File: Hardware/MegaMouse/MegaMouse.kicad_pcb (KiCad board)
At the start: 2 copper layers, 93 x 120.5 mm, 12 parts, among them J201 Motor, J301 Motor, U101 ATmega328P-A, U102 STATE, U201 DRV8871DDA, U301 DRV8871DDA

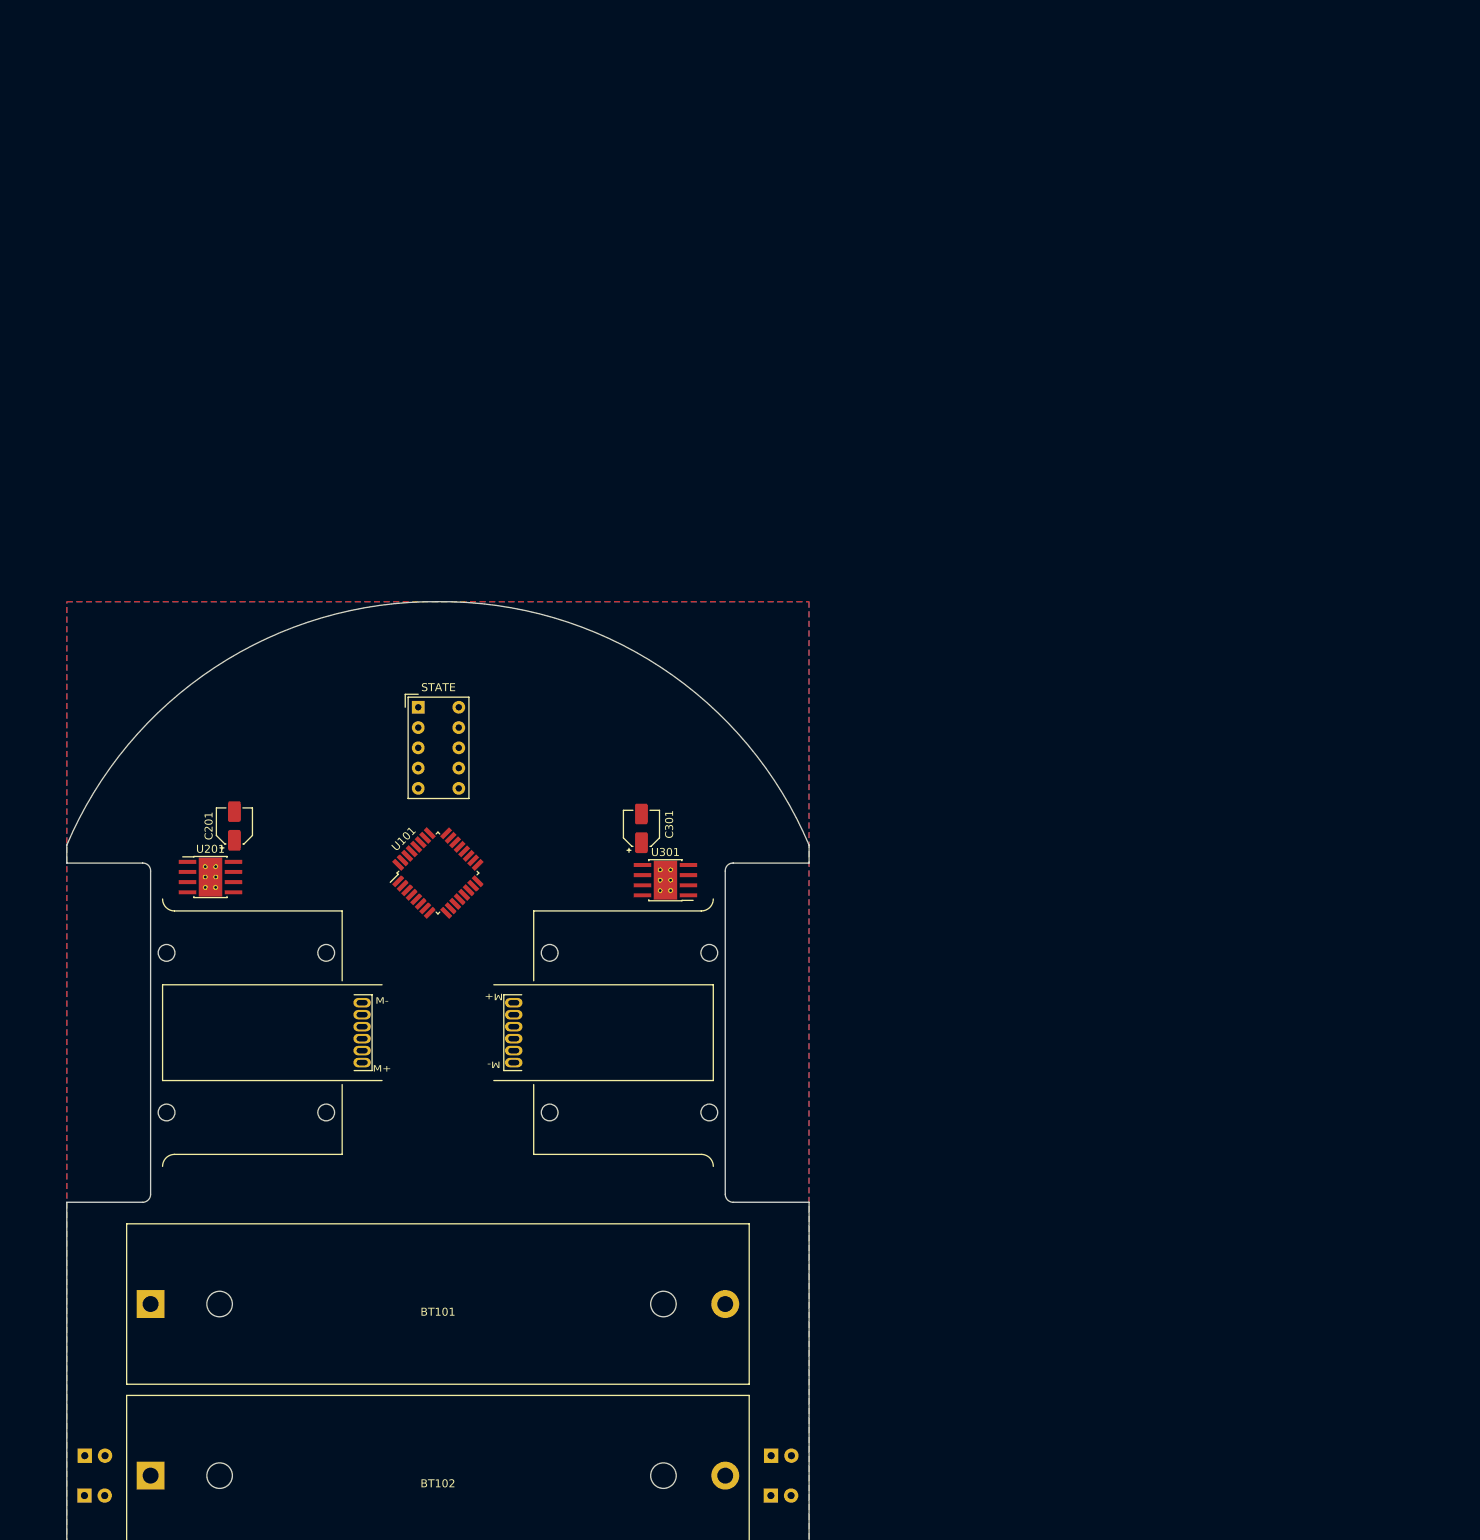
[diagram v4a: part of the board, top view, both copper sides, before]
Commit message: Add second layer
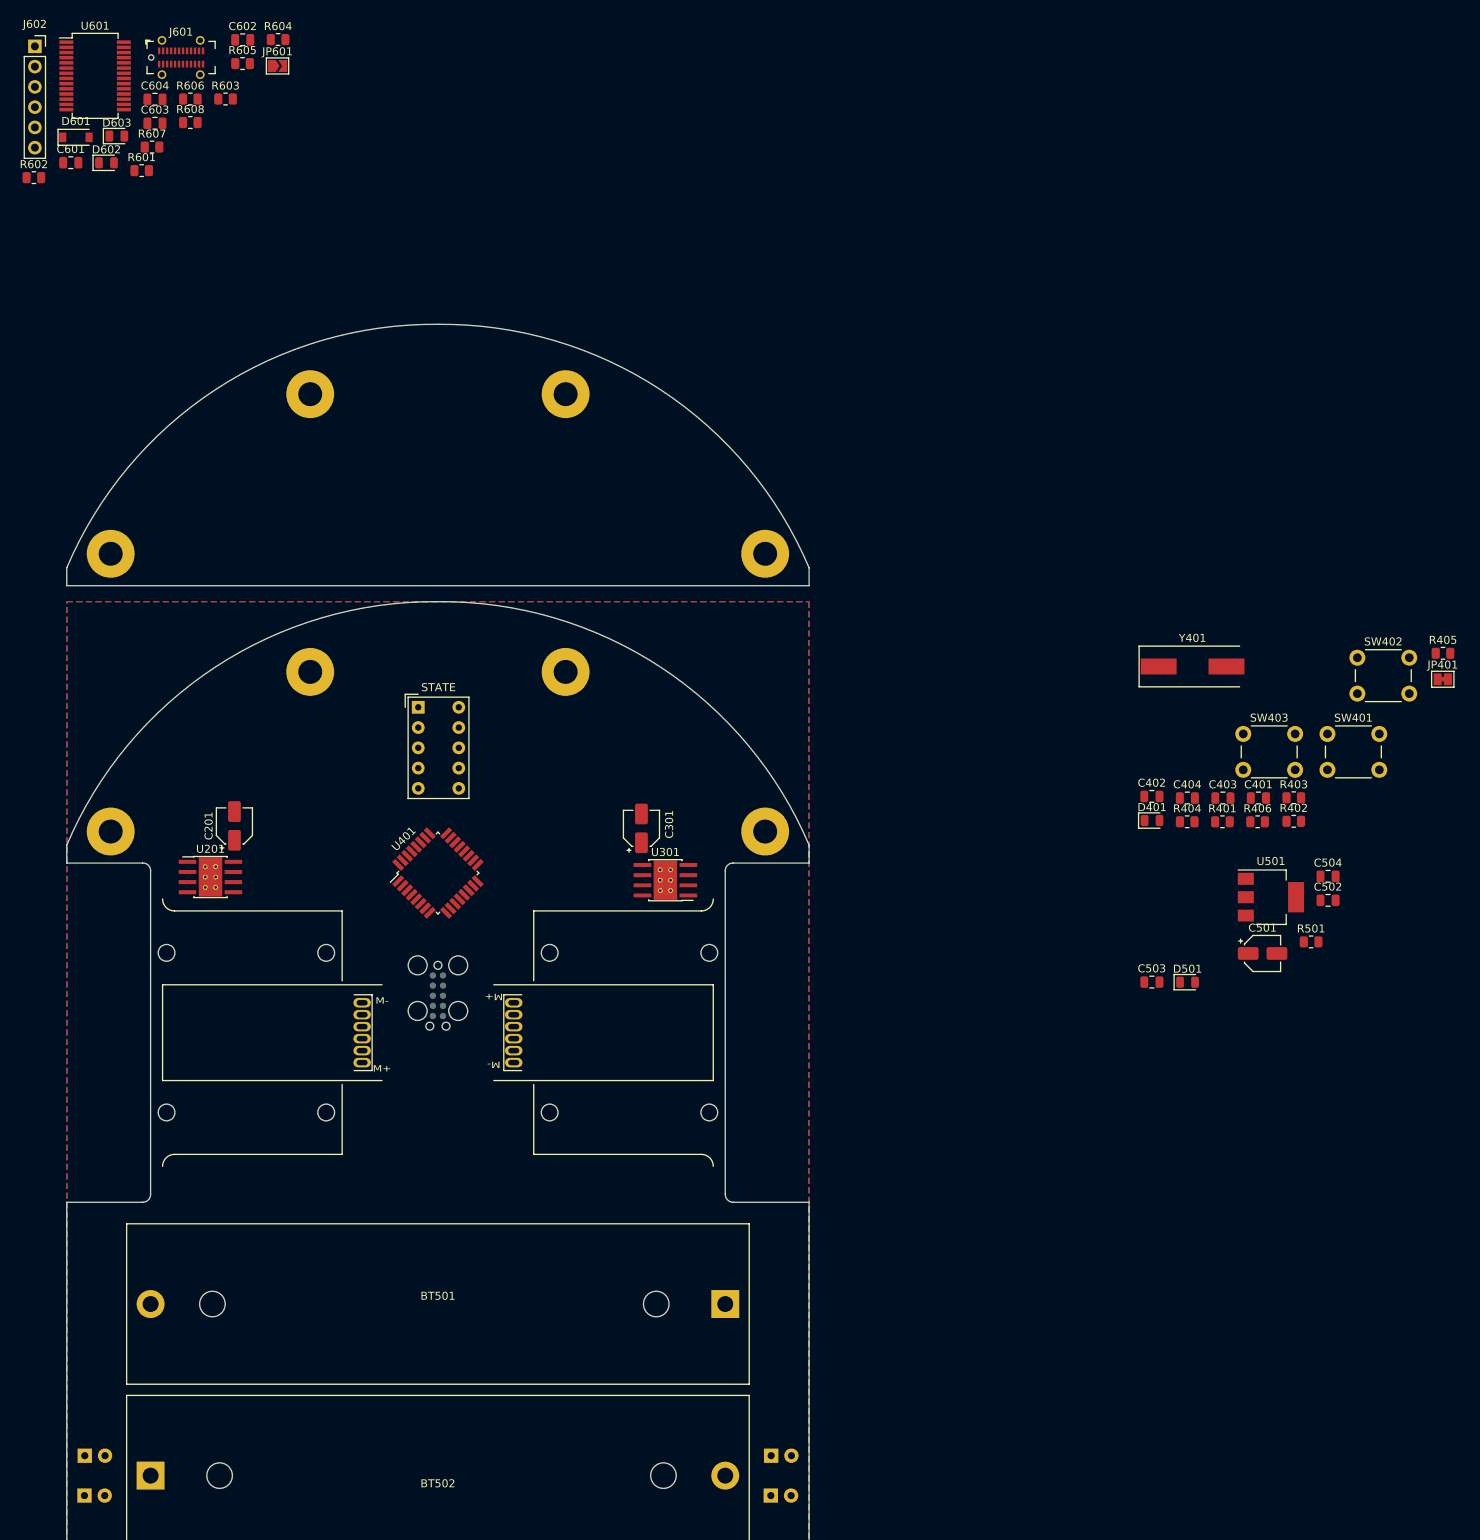
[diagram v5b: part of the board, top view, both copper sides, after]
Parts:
- removed BT101: Cell1, Battery:BatteryHolder_MPD_BH-18650-PC2
- removed BT102: Cell2, Battery:BatteryHolder_MPD_BH-18650-PC2
- removed the U101 at (0.00, -20.0)
- added BT501: Cell1, Battery:BatteryHolder_MPD_BH-18650-PC2, F.Cu at (36.0, 34.0)
- added BT502: Cell2, Battery:BatteryHolder_MPD_BH-18650-PC2, F.Cu at (-36.0, 55.5)
- added C401: 100nF, Capacitor_SMD:C_0805_2012Metric, F.Cu at (102.8, -29.4)
- added C402: 100nF, Capacitor_SMD:C_0805_2012Metric, F.Cu at (89.5, -29.6)
- added C403: 22pf, Capacitor_SMD:C_0805_2012Metric, F.Cu at (98.3, -29.4)
- added C404: 22pf, Capacitor_SMD:C_0805_2012Metric, F.Cu at (93.9, -29.4)
- added C501: 10uf, Capacitor_SMD:CP_Elec_4x3, F.Cu at (103.3, -9.92)
- added C502: 100nF, Capacitor_SMD:C_0805_2012Metric, F.Cu at (111.5, -16.6)
- added C503: 100nF, Capacitor_SMD:C_0805_2012Metric, F.Cu at (89.5, -6.34)
- added C504: 1uF, Capacitor_SMD:C_0805_2012Metric, F.Cu at (111.5, -19.6)
- added C601: 100nF, Capacitor_SMD:C_0805_2012Metric, F.Cu at (-46.0, -109.0)
- added C602: 100nF, Capacitor_SMD:C_0805_2012Metric, F.Cu at (-24.5, -124.4)
- added C603: 100nF, Capacitor_SMD:C_0805_2012Metric, F.Cu at (-35.5, -113.9)
- added C604: 100nF, Capacitor_SMD:C_0805_2012Metric, F.Cu at (-35.5, -117.0)
- added D401: STAT, LED_SMD:LED_0805_2012Metric, F.Cu at (89.5, -26.6)
- added D501: PWR, LED_SMD:LED_0805_2012Metric, F.Cu at (93.9, -6.33)
- added D601: MBR0520, Diode_SMD:D_SOD-123, F.Cu at (-45.4, -112.2)
- added D602: RX, LED_SMD:LED_0805_2012Metric, F.Cu at (-41.5, -109.0)
- added D603: TX, LED_SMD:LED_0805_2012Metric, F.Cu at (-40.2, -112.3)
- added H101: MountingHole_Pad, MountingHole:MountingHole_3mm_Pad, F.Cu at (41.0, -25.2)
- added H102: MountingHole_Pad, MountingHole:MountingHole_3mm_Pad, F.Cu at (-16.0, -45.2)
- added H103: MountingHole_Pad, MountingHole:MountingHole_3mm_Pad, F.Cu at (-41.0, -25.2)
- added H104: MountingHole_Pad, MountingHole:MountingHole_3mm_Pad, F.Cu at (16.0, -45.2)
- added H601: MountingHole_Pad, MountingHole:MountingHole_3mm_Pad, F.Cu at (41.0, -60.0)
- added H602: MountingHole_Pad, MountingHole:MountingHole_3mm_Pad, F.Cu at (16.0, -80.0)
- added H603: MountingHole_Pad, MountingHole:MountingHole_3mm_Pad, F.Cu at (-41.0, -60.0)
- added H604: MountingHole_Pad, MountingHole:MountingHole_3mm_Pad, F.Cu at (-16.0, -80.0)
- added J401: ICSP, Connector:Tag-Connect_TC2050-IDC-FP_2x05_P1.27mm_Vertical, B.Cu at (0.00, -4.62)
- added J601: USBC, Connector_USB:USB_C_Receptacle_GCT_USB4115-03-C, F.Cu at (-32.2, -122.2)
- added J602: PROG, Connector_PinSocket_2.54mm:PinSocket_1x06_P2.54mm_Vertical, F.Cu at (-50.5, -123.6)
- added JP401: RSTBridge, Jumper:SolderJumper-2_P1.3mm_Bridged_Pad1.0x1.5mm, F.Cu at (125.9, -44.3)
- added JP601: SolderJumper_2_Open, Jumper:SolderJumper-2_P1.3mm_Open_TrianglePad1.0x1.5mm, F.Cu at (-20.1, -121.1)
- added R401: 1K, Resistor_SMD:R_0805_2012Metric, F.Cu at (98.3, -26.4)
- added R402: 1K, Resistor_SMD:R_0805_2012Metric, F.Cu at (107.2, -26.5)
- added R403: 1K, Resistor_SMD:R_0805_2012Metric, F.Cu at (107.2, -29.4)
- added R404: 1K, Resistor_SMD:R_0805_2012Metric, F.Cu at (93.9, -26.4)
- added R405: 10K, Resistor_SMD:R_0805_2012Metric, F.Cu at (125.9, -47.5)
- added R406: 10K, Resistor_SMD:R_0805_2012Metric, F.Cu at (102.7, -26.4)
- added R501: 1K, Resistor_SMD:R_0805_2012Metric, F.Cu at (109.4, -11.4)
- added R601: 5K1, Resistor_SMD:R_0805_2012Metric, F.Cu at (-37.1, -108.0)
- added R602: 5K1, Resistor_SMD:R_0805_2012Metric, F.Cu at (-50.6, -107.1)
- added R603: 4K7, Resistor_SMD:R_0805_2012Metric, F.Cu at (-26.6, -117.0)
- added R604: 10K, Resistor_SMD:R_0805_2012Metric, F.Cu at (-20.0, -124.4)
- added R605: 22R, Resistor_SMD:R_0805_2012Metric, F.Cu at (-24.5, -121.4)
- added R606: 22R, Resistor_SMD:R_0805_2012Metric, F.Cu at (-31.0, -117.0)
- added R607: 1K, Resistor_SMD:R_0805_2012Metric, F.Cu at (-35.8, -111.0)
- added R608: 1K, Resistor_SMD:R_0805_2012Metric, F.Cu at (-31.0, -114.0)
- added SW401: RESET, Button_Switch_THT:SW_PUSH_6mm_H5mm, F.Cu at (111.5, -37.4)
- added SW402: START_SW, Button_Switch_THT:SW_PUSH_6mm_H5mm, F.Cu at (115.2, -47.0)
- added SW403: STOP/MODE_SW, Button_Switch_THT:SW_PUSH_6mm_H5mm, F.Cu at (100.9, -37.4)
- added U401: ATmega328P, Package_QFP:TQFP-32_7x7mm_P0.8mm, F.Cu at (0.00, -20.0)
- added U501: NCV1117ST50T3G, Package_TO_SOT_SMD:SOT-223, F.Cu at (104.4, -17.0)
- added U601: FT232RL, Package_SO:SSOP-28_5.3x10.2mm_P0.65mm, F.Cu at (-43.0, -119.9)
- added Y401: 16mHz, Crystal:Crystal_SMD_HC49-SD, F.Cu at (94.5, -45.9)
- renumbered U102 to U101
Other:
- board size 93 x 120.5 mm -> 93 x 155.2 mm

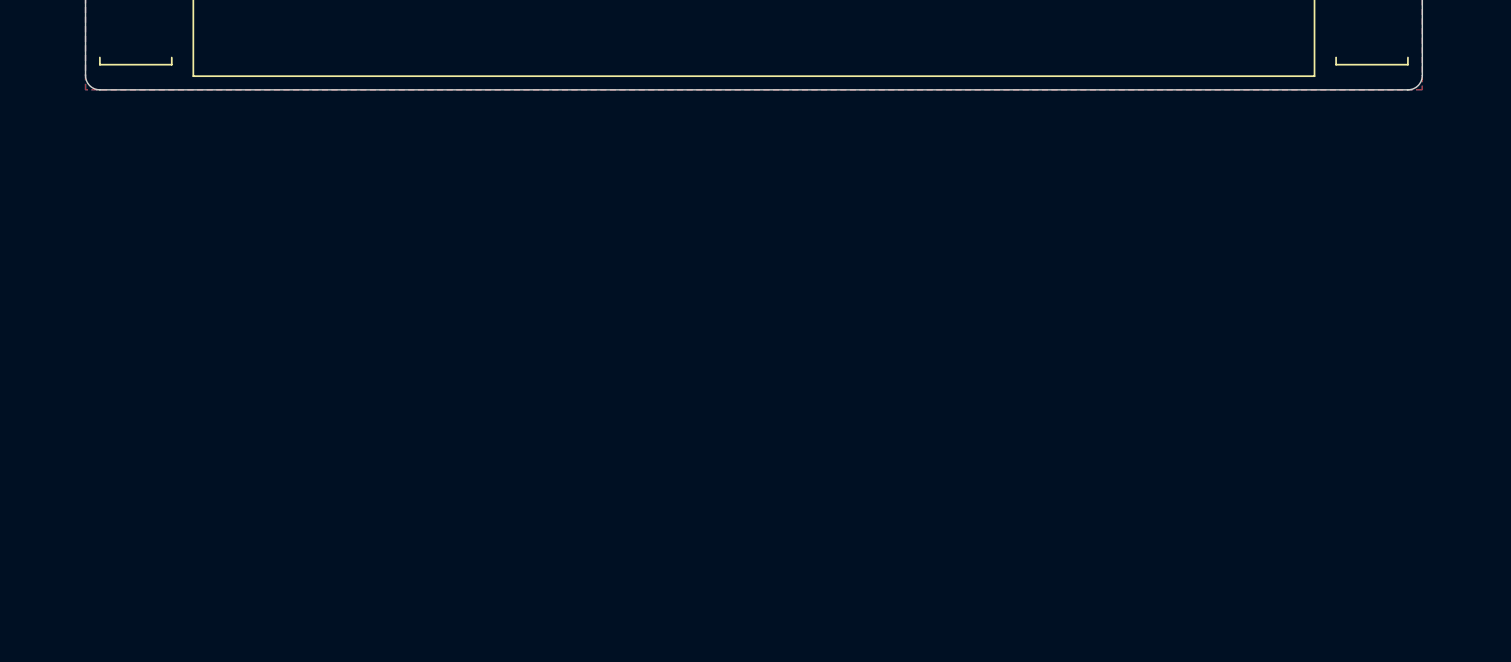
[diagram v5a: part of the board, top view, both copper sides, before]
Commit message: Add panelization
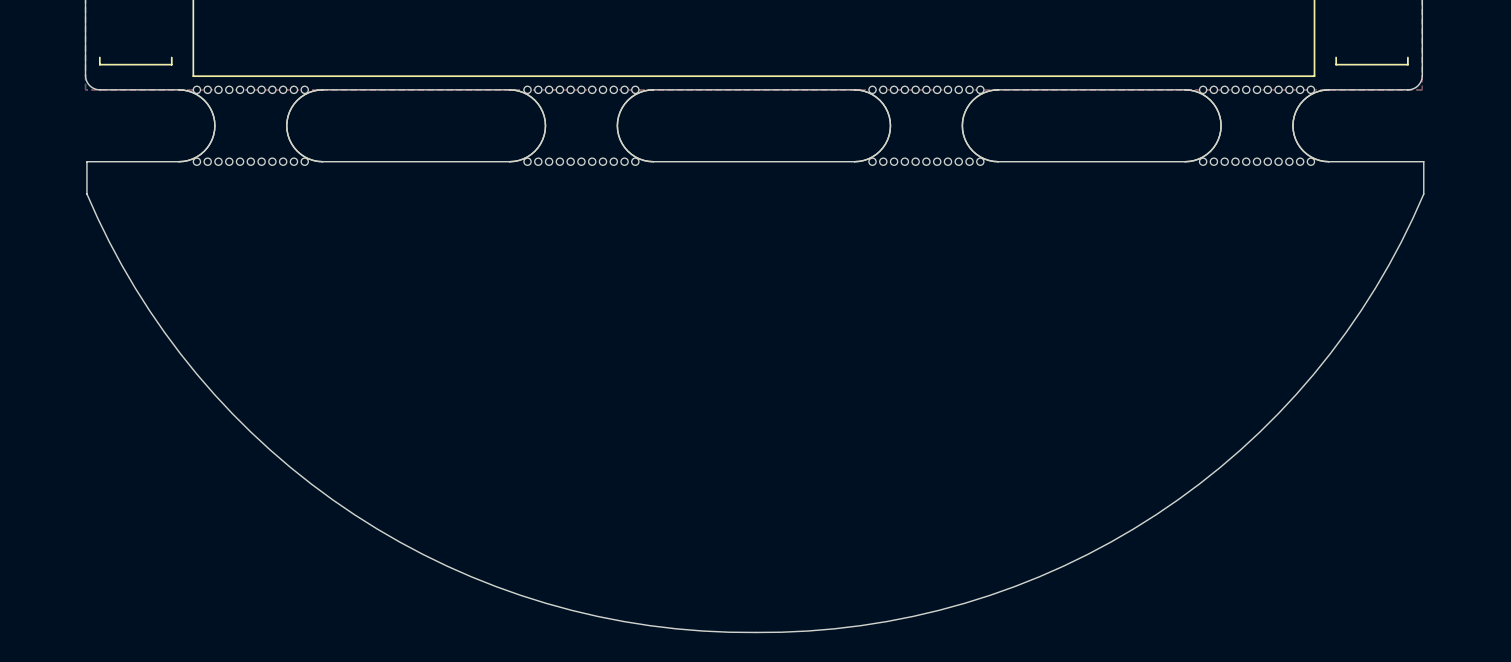
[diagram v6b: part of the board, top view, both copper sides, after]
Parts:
- added mouse-bite-5mm-slot: VAL**, Panelization:mouse-bite-5mm-slot, F.Cu at (-35.0, 69.0)
- added mouse-bite-5mm-slot: VAL**, Panelization:mouse-bite-5mm-slot, F.Cu at (35.0, 69.0)
- added mouse-bite-5mm-slot: VAL**, Panelization:mouse-bite-5mm-slot, F.Cu at (-12.0, 69.0)
- added mouse-bite-5mm-slot: VAL**, Panelization:mouse-bite-5mm-slot, F.Cu at (12.0, 69.0)
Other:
- board size 93 x 155.2 mm -> 93.1 x 193 mm
